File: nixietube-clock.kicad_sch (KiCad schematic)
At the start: 4 parts

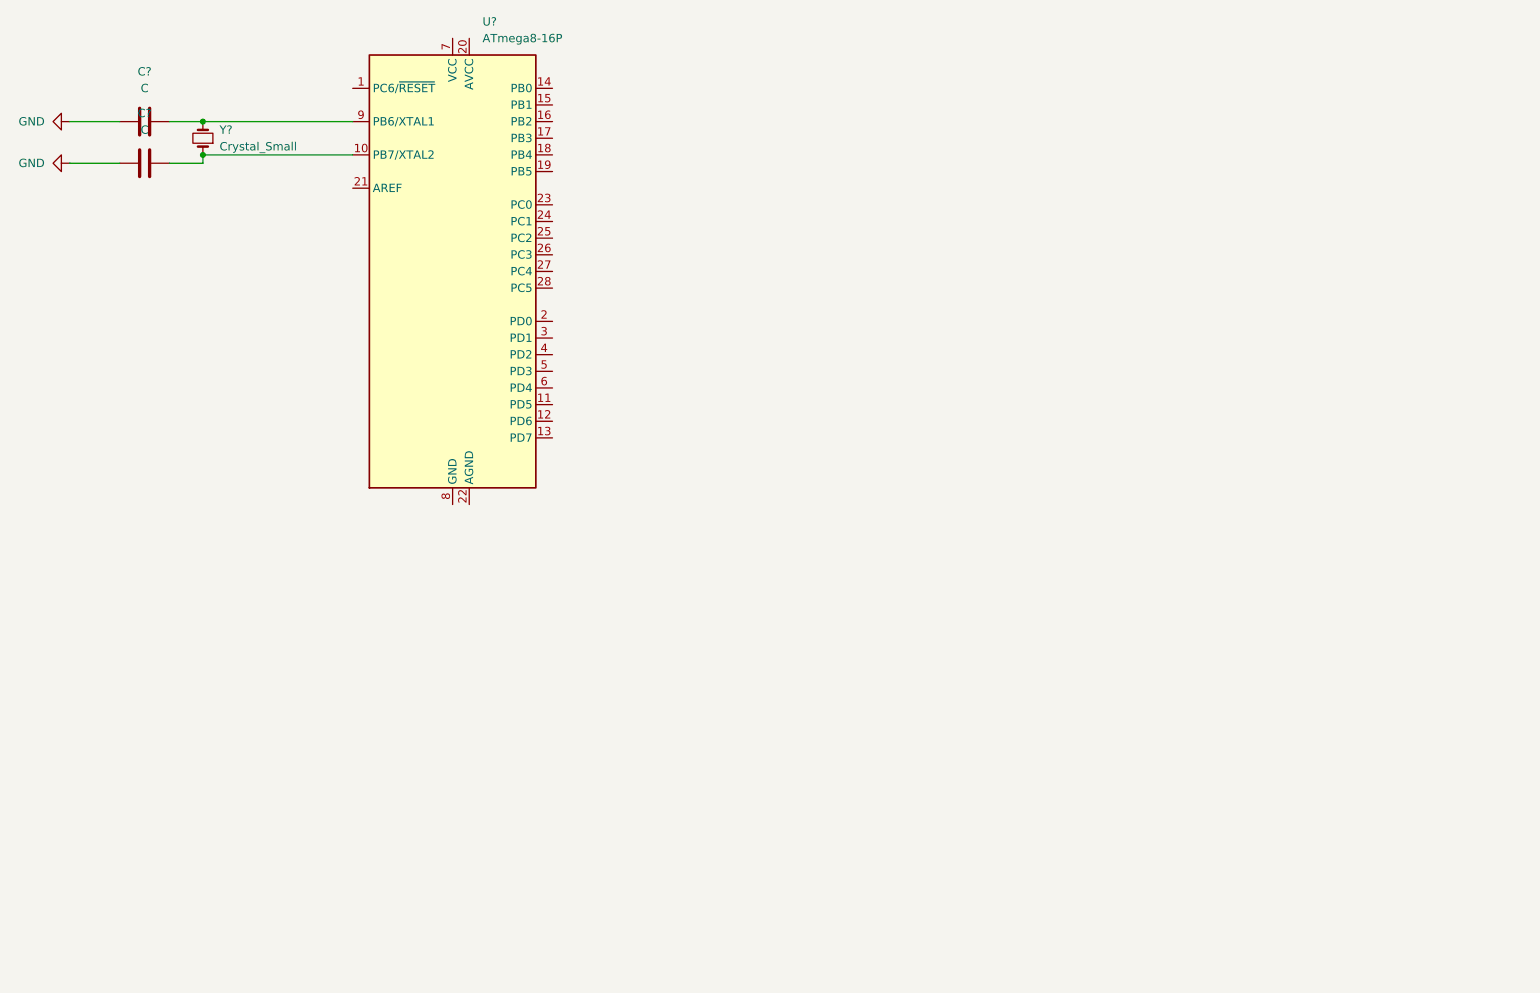
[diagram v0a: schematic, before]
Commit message: Add hiracical schematics and nixie symbols and footprints
The hiracichal schematics added are:
- power: DC-DC high voltage power converter
- mcu: atmega8 microcontroller
- input: user input, knobs and buttons
- nixies: the in-14 nixie tubes and k155na1 nixie tube controllers

Added symbols and footprints for the in-14 tubes and k155na1
controllers.
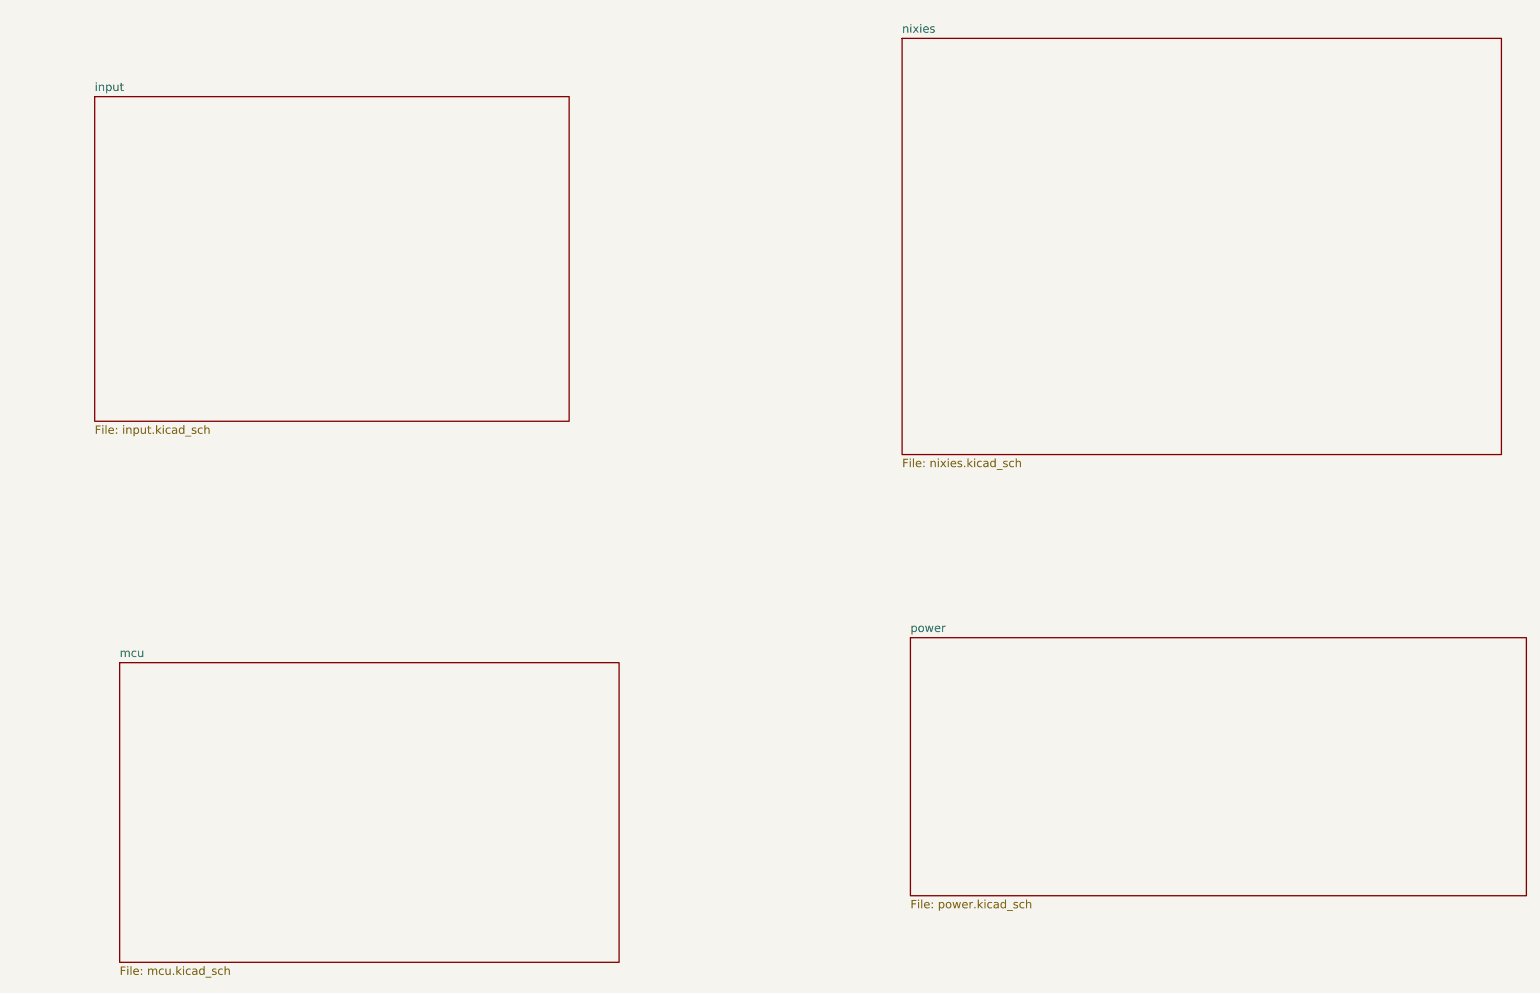
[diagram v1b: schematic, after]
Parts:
- removed C? (x2): C, symbol Device:C
- removed U?: ATmega8-16P, Package_DIP:DIP-28_W7.62mm, symbol MCU_Microchip_ATmega:ATmega8-16P
- removed Y?: Crystal_Small, symbol Device:Crystal_Small
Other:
- added sheet input (input.kicad_sch)
- added sheet mcu (mcu.kicad_sch)
- added sheet nixies (nixies.kicad_sch)
- added sheet power (power.kicad_sch)
